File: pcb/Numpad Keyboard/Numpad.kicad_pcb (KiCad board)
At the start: 2 copper layers, 82.4 x 128 mm, 61 parts, among them U1 MCP23S17_SO, U2 IS31FL3743-QF, U3 IS31FL3743-QF

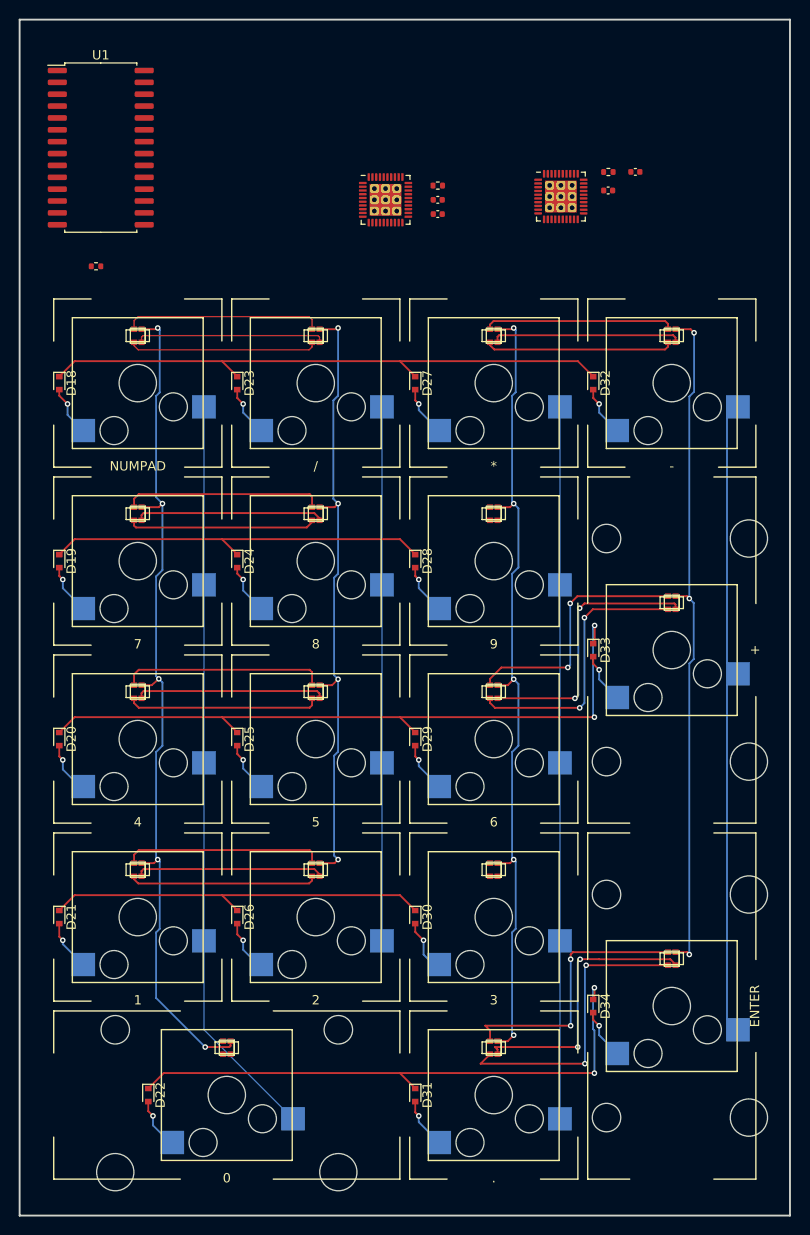
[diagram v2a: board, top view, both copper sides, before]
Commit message: Added more tracks to numpad and positioned LED controllers
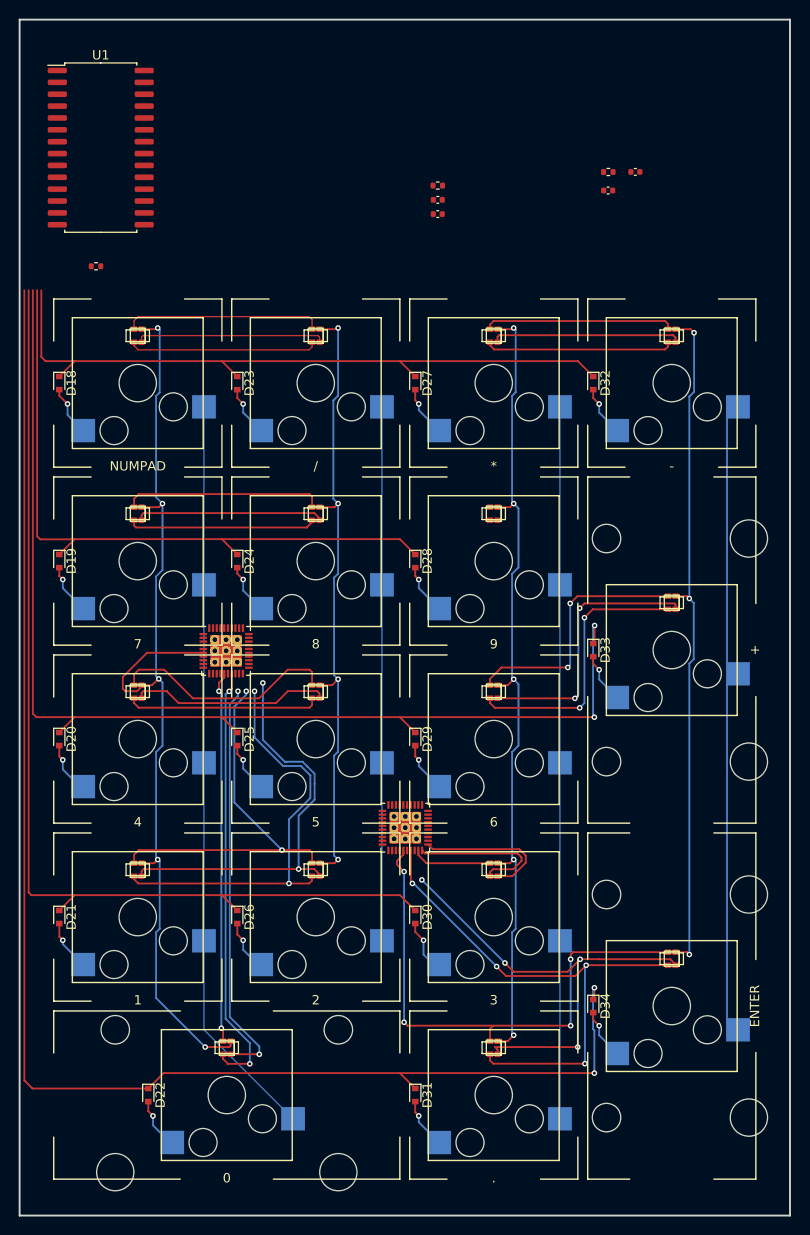
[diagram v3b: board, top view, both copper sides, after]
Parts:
- moved U3 69.6 mm to (63.1, 109.3)
- moved U2 51.2 mm to (43.9, 90.4)
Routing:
- net Net-(D22-Pad1): track 61.2 -> 159.4 mm
- net Net-(D21-Pad1): track 41.8 -> 111.3 mm
- net Net-(D20-Pad1): track 74.3 -> 124.3 mm
- net Net-(D5-Pad2): track 0.00 -> 46.8 mm, vias 0 -> 2
- net Net-(D5-Pad4): track 0.00 -> 43.6 mm, vias 0 -> 2
- net Net-(D5-Pad1): track 0.00 -> 39.7 mm, vias 0 -> 2
- net Net-(D19-Pad1): track 41.8 -> 72.3 mm
- net Net-(D14-Pad1): track 29.2 -> 56.9 mm, vias 2 -> 4
- net Net-(D17-Pad2): track 31.9 -> 57.1 mm, vias 2 -> 4
- net Net-(D4-Pad2): track 20.1 -> 45.3 mm, vias 0 -> 2
- net Net-(D4-Pad4): track 20.1 -> 44.2 mm, vias 0 -> 2
- net Net-(D14-Pad4): track 29.7 -> 51.3 mm, vias 2 -> 4
- net Net-(D4-Pad1): track 21.4 -> 41.0 mm, vias 0 -> 2
- net Net-(D13-Pad2): track 0.00 -> 15.6 mm
- net Net-(D13-Pad4): track 0.00 -> 15.3 mm
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
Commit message: Fixed constraints
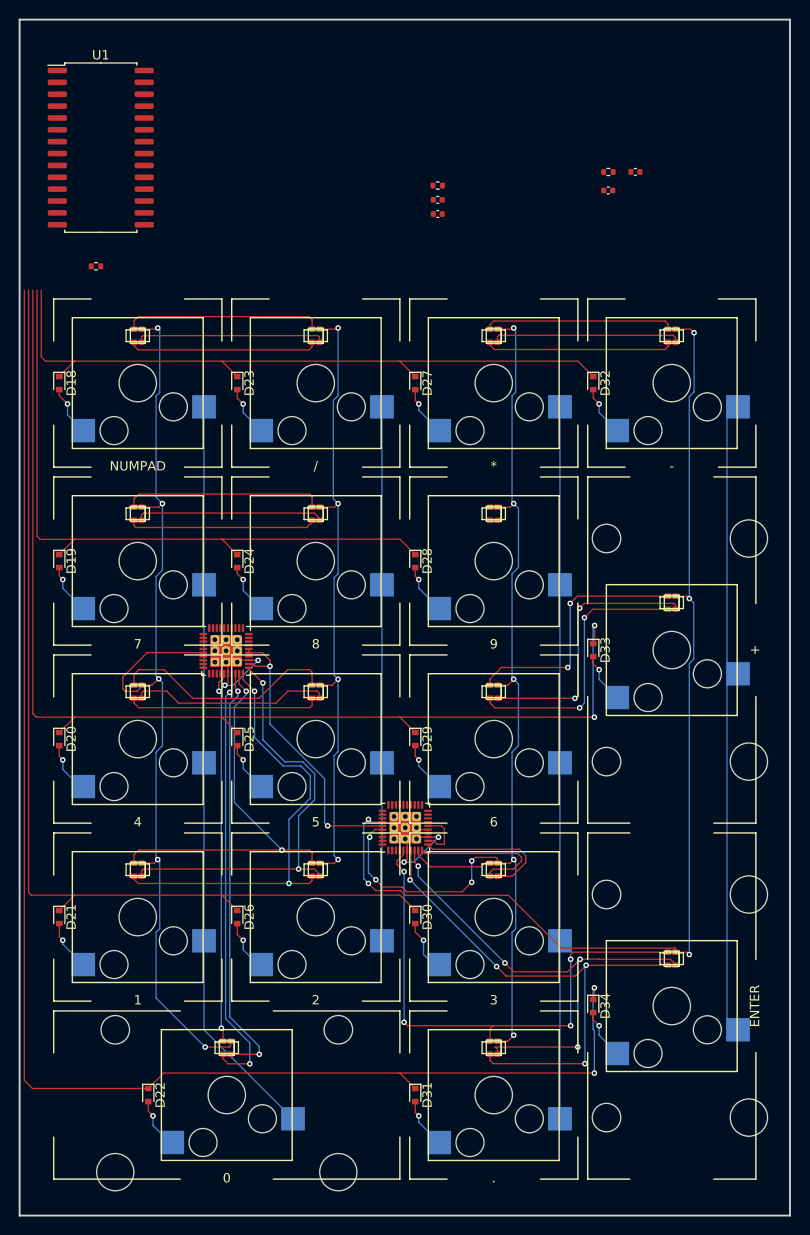
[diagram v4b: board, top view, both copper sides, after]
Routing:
- net Net-(D15-Pad3): track 72.5 -> 117.5 mm, vias 3 -> 5
- net Net-(R1-Pad1): track 0.00 -> 37.5 mm, vias 0 -> 2
- net Net-(D10-Pad3): track 87.0 -> 110.8 mm, vias 5 -> 9
- net Net-(R2-Pad1): track 0.00 -> 23.2 mm, vias 0 -> 4
- net Net-(D14-Pad4): track 51.3 -> 54.8 mm
- net Net-(D4-Pad2): track 45.3 -> 47.7 mm
- net Net-(D4-Pad4): track 44.2 -> 46.4 mm
- net Net-(D4-Pad1): track 41.0 -> 43.2 mm
- net Net-(D5-Pad4): track 43.6 -> 45.6 mm

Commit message: Numpad has all tracks now.
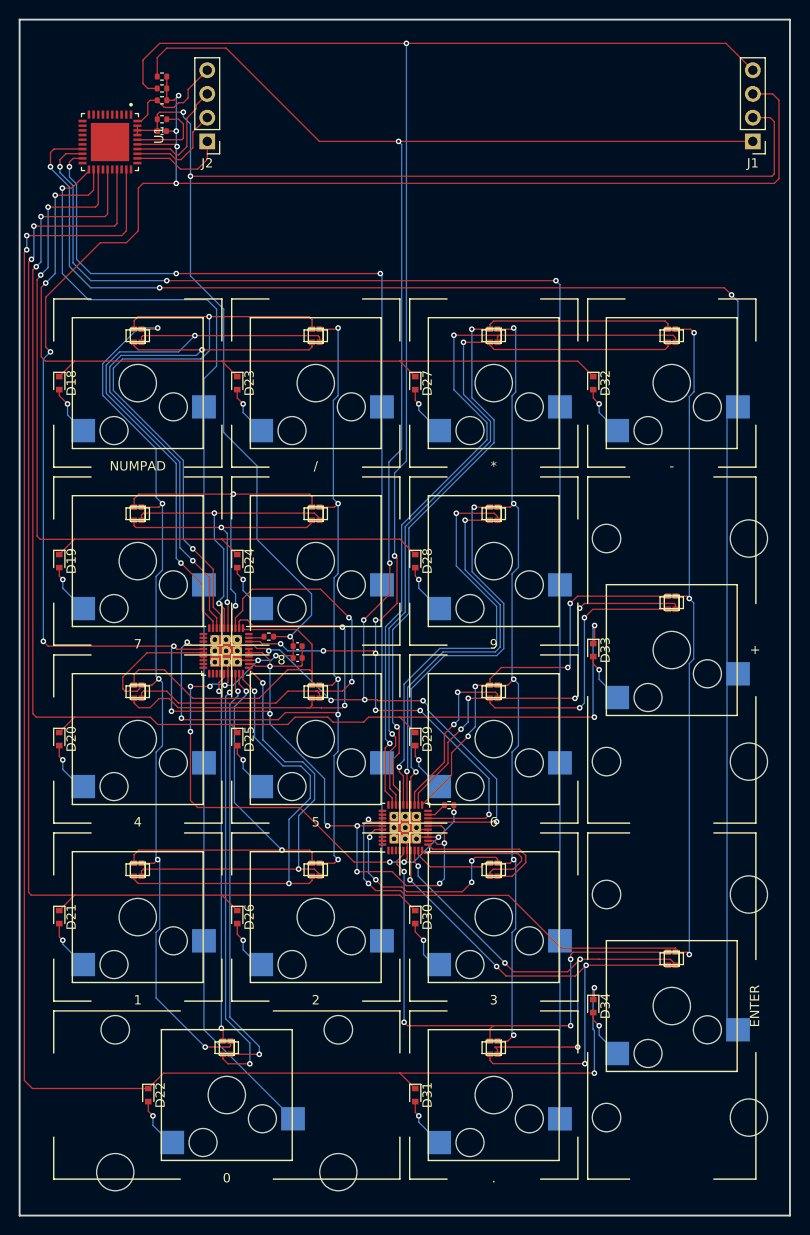
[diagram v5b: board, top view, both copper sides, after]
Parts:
- removed C3: C 1uF, Footprints:C_0402_1005Metric
- removed C4: C_100nF, Footprints:C_0402_1005Metric
- added C5: C_47nF, Footprints:C_0402_1005Metric, F.Cu at (37.1, 34.8)
- added J1: Conn_01x04, Connector_PinHeader_2.54mm:PinHeader_1x04_P2.54mm_Vertical, F.Cu at (100.3, 35.9)
- added J2: Conn_01x04, Connector_PinHeader_2.54mm:PinHeader_1x04_P2.54mm_Vertical, F.Cu at (41.9, 35.9)
- added R4: R 10 kOhm, Footprints:R_0402_1005Metric, F.Cu at (37.1, 29.0)
- added R5: R 10 kOhm, Footprints:R_0402_1005Metric, F.Cu at (37.1, 30.2)
- added R6: R 10 kOhm, Footprints:R_0402_1005Metric, F.Cu at (37.1, 31.5)
- R1: value R -> R_39_kOhm
- U1: value MCP23S17_SO -> MAX7301ATL+; footprint Package_SO:SOIC-28W_7.5x17.9mm_P1.27mm -> Footprints:QFN50P600X600X80-41N
- moved R3 69.9 mm to (67.8, 106.9), turned to 180 degrees
- moved R2 51.6 mm to (48.5, 88.9), turned to 180 degrees
- moved C1 51.3 mm to (51.6, 91.2), turned to 180 degrees
- moved C2 48.6 mm to (51.6, 89.9), turned to 180 degrees
- moved R1 17.2 mm to (37.1, 33.5)
- moved U1 1.15 mm to (31.5, 36.0), turned to -90 degrees
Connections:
- C1 pad 1: Net-(R1-Pad1) -> Net-(C1-Pad1)
- C1 pad 2: Net-(R2-Pad1) -> Net-(C1-Pad2)
- C2 pad 1: Net-(R1-Pad1) -> Net-(C1-Pad1)
- C2 pad 2: Net-(R2-Pad1) -> Net-(C1-Pad2)
- R1 pad 2: Net-(R1-Pad2) -> Net-(C1-Pad2)
- R2 pad 1: Net-(R2-Pad1) -> Net-(C1-Pad2)
- R3 pad 1: Net-(R2-Pad1) -> Net-(C1-Pad2)
- U1 pad 10: Net-(R2-Pad1) -> unconnected-(U1-Pad10)
- U1 pad 15: Net-(R2-Pad1) -> unconnected-(U1-Pad15)
- U1 pad 16: Net-(R1-Pad1) -> unconnected-(U1-Pad16)
- U1 pad 17: Net-(R1-Pad1) -> Net-(K_ENTER1-Pad1)
- U1 pad 18: Net-(R1-Pad2) -> Net-(K_DOT1-Pad1)
- U1 pad 19: unconnected-(U1-Pad19) -> Net-(K_EIGHT1-Pad1)
- U1 pad 21: Net-(D18-Pad1) -> Net-(K_FOUR1-Pad1)
- U1 pad 22: Net-(D19-Pad1) -> Net-(D18-Pad1)
- U1 pad 23: Net-(D20-Pad1) -> Net-(D19-Pad1)
- U1 pad 24: Net-(D21-Pad1) -> unconnected-(U1-Pad24)
- U1 pad 25: Net-(D22-Pad1) -> Net-(D20-Pad1)
- U1 pad 27: unconnected-(U1-Pad27) -> Net-(D21-Pad1)
- U1 pad 5: Net-(K_ENTER1-Pad1) -> unconnected-(U1-Pad5)
- U1 pad 6: Net-(K_DOT1-Pad1) -> unconnected-(U1-Pad6)
- U1 pad 7: Net-(K_EIGHT1-Pad1) -> unconnected-(U1-Pad7)
- U1 pad 8: Net-(K_FOUR1-Pad1) -> unconnected-(U1-Pad8)
- U1 pad 9: Net-(R1-Pad1) -> unconnected-(U1-Pad9)
- U2 pad 16: Net-(R2-Pad1) -> Net-(C1-Pad2)
- U2 pad 22: Net-(R1-Pad1) -> Net-(C1-Pad1)
- U2 pad 23: Net-(R2-Pad1) -> Net-(C1-Pad2)
- U2 pad 24: Net-(R1-Pad1) -> Net-(C1-Pad1)
- U2 pad 25: Net-(R1-Pad1) -> Net-(C1-Pad1)
- U2 pad 26: Net-(R1-Pad1) -> Net-(C1-Pad1)
- U2 pad 27: unconnected-(U2-Pad27) -> Net-(U3-Pad27)
- U2 pad 28: unconnected-(U2-Pad28) -> Net-(U3-Pad28)
- U2 pad 5: Net-(R1-Pad1) -> Net-(C1-Pad1)
- U3 pad 16: Net-(R2-Pad1) -> Net-(C1-Pad2)
- U3 pad 22: Net-(R1-Pad1) -> Net-(C1-Pad1)
- U3 pad 23: Net-(R2-Pad1) -> Net-(C1-Pad2)
- U3 pad 24: Net-(R2-Pad1) -> Net-(C1-Pad2)
- U3 pad 25: Net-(R2-Pad1) -> Net-(C1-Pad2)
- U3 pad 26: Net-(R1-Pad1) -> Net-(C1-Pad1)
- U3 pad 27: unconnected-(U3-Pad27) -> Net-(U3-Pad27)
- U3 pad 28: unconnected-(U3-Pad28) -> Net-(U3-Pad28)
- U3 pad 5: Net-(R1-Pad1) -> Net-(C1-Pad1)
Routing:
- net Net-(C1-Pad1): track 0.00 -> 251.3 mm, vias 0 -> 15
- net Net-(C1-Pad2): track 0.00 -> 216.9 mm, vias 0 -> 13
- net Net-(U3-Pad28): track 0.00 -> 184.5 mm, vias 0 -> 9
- net Net-(U3-Pad27): track 0.00 -> 176.8 mm, vias 0 -> 8
- net Net-(K_ENTER1-Pad1): track 68.6 -> 163.0 mm, vias 0 -> 3
- net Net-(K_DOT1-Pad1): track 76.2 -> 156.7 mm, vias 0 -> 3
- net Net-(D10-Pad4): track 20.3 -> 82.1 mm, vias 0 -> 2
- net Net-(K_EIGHT1-Pad1): track 57.1 -> 116.9 mm, vias 0 -> 3
- net Net-(D10-Pad1): track 20.4 -> 79.6 mm, vias 0 -> 2
- net Net-(D10-Pad2): track 20.1 -> 79.0 mm, vias 0 -> 2
- net Net-(D1-Pad1): track 21.3 -> 68.6 mm, vias 0 -> 2
- net Net-(D11-Pad4): track 0.00 -> 45.8 mm, vias 0 -> 2
- net Net-(D1-Pad4): track 20.3 -> 64.0 mm, vias 0 -> 2
- net Net-(D1-Pad2): track 20.2 -> 63.6 mm, vias 0 -> 2
- net Net-(D11-Pad1): track 0.00 -> 42.9 mm, vias 0 -> 2
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
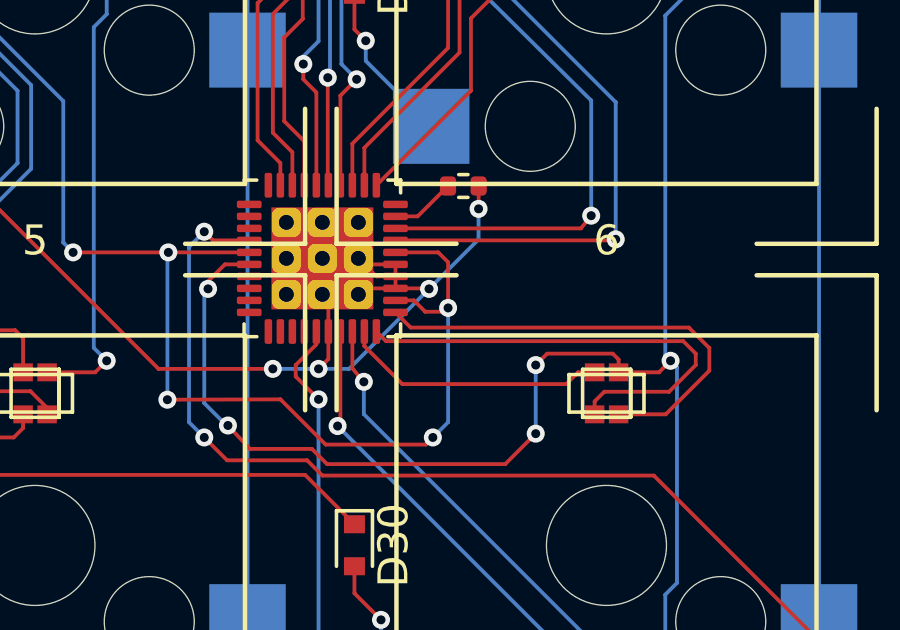
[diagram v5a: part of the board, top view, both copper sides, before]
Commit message: Fixed errors in DRC for PCB
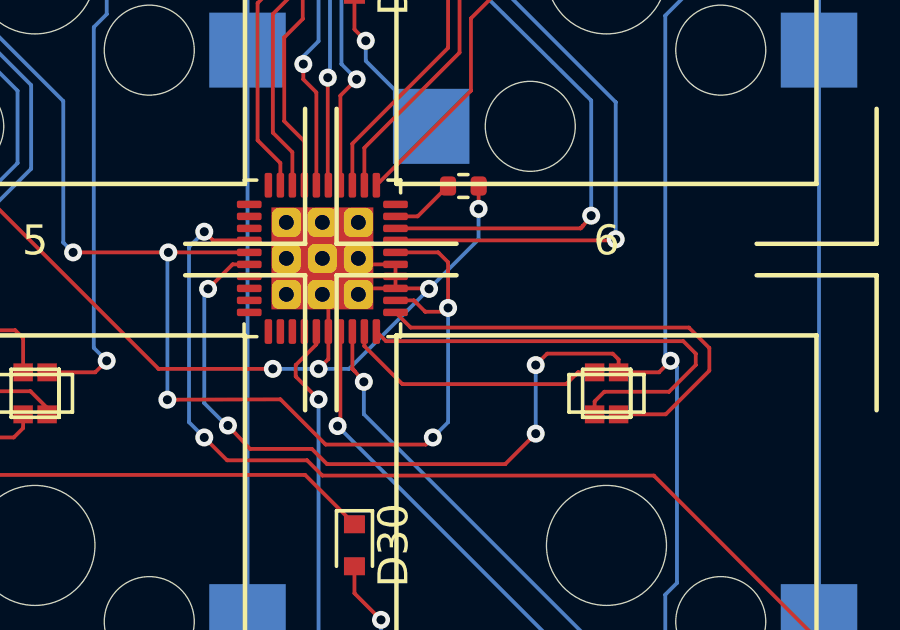
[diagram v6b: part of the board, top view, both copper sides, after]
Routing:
- net Net-(C1-Pad2): track 216.9 -> 219.0 mm

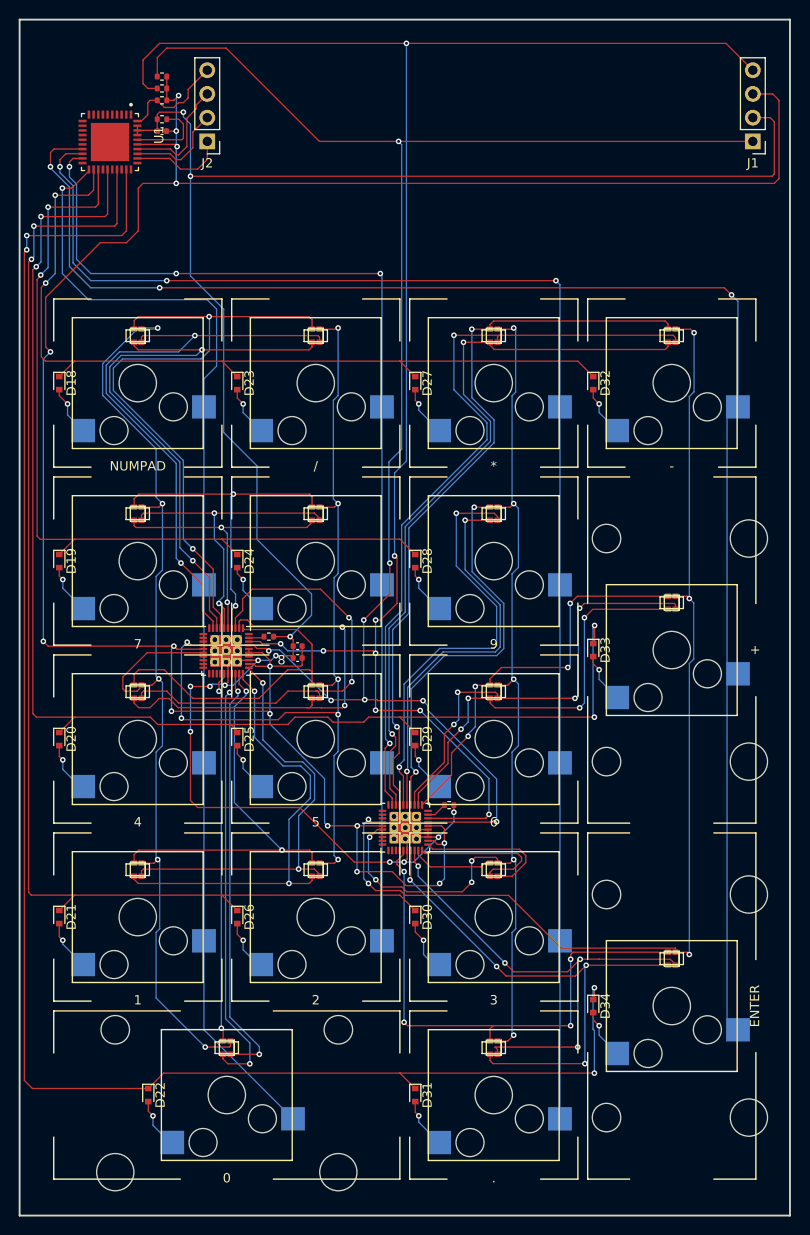
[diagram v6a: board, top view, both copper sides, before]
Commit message: Modified footprint for LEDs, so they have right rotation for pick and place
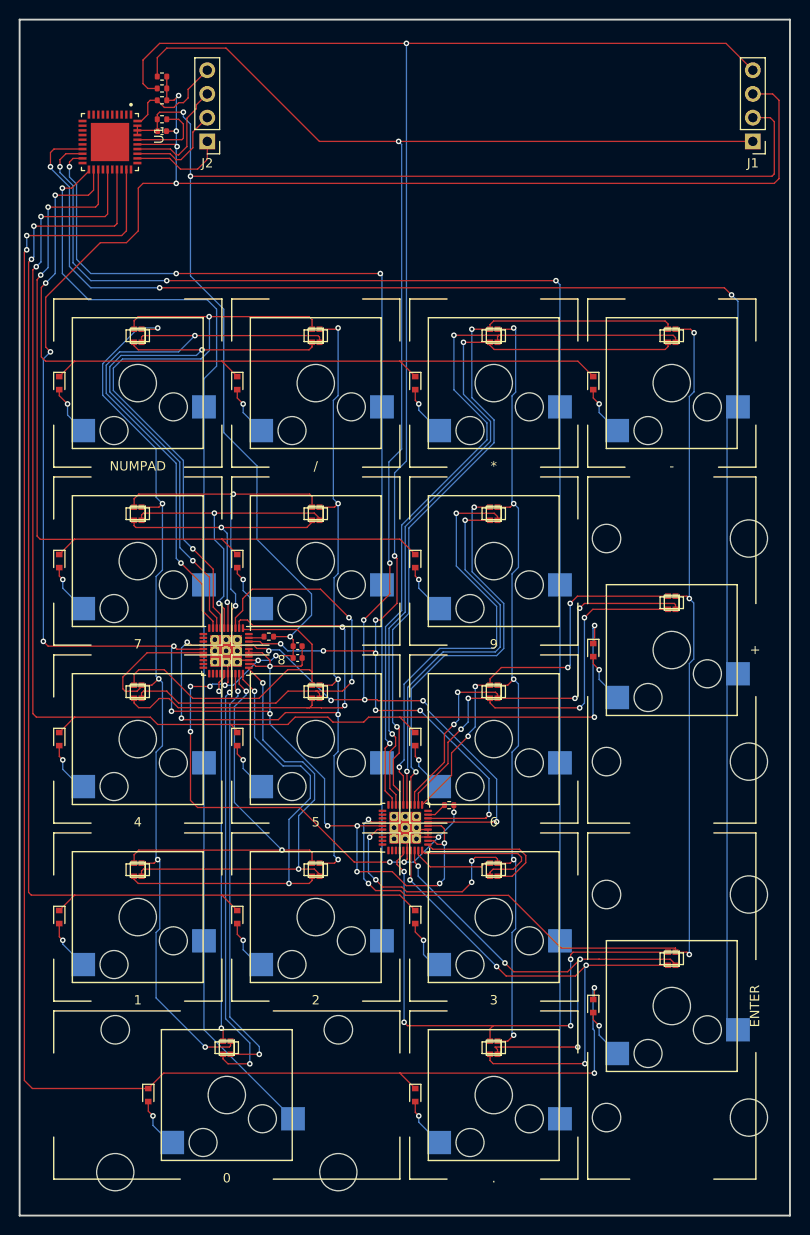
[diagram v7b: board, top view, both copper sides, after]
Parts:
- D18, D19, D20, D21, D22, D23, D24, D25, D26, D27, D28, D29, D30, D31, D32, D33, D34: footprint Diode_SMD:D_SOD-523 -> Footprints:D_SOD-523
- turned D1 to 0 degrees
- turned D10 to 0 degrees
- turned D11 to 0 degrees
- turned D12 to 0 degrees
- turned D13 to 0 degrees
- turned D14 to 0 degrees
- turned D15 to 0 degrees
- turned D16 to 0 degrees
- turned D17 to 0 degrees
- turned D3 to 0 degrees
- turned D4 to 0 degrees
- turned D5 to 0 degrees
- turned D6 to 0 degrees
- turned D7 to 0 degrees
- turned D8 to 0 degrees
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- renumbered D2 to De
